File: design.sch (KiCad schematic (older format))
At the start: 21 parts, among them J1 USB_C_Receptacle, J2 Conn_01x05, Q1 2N7002K, Q2 2N7002K, Q3 2N7002K, U1 ATtiny814-SS

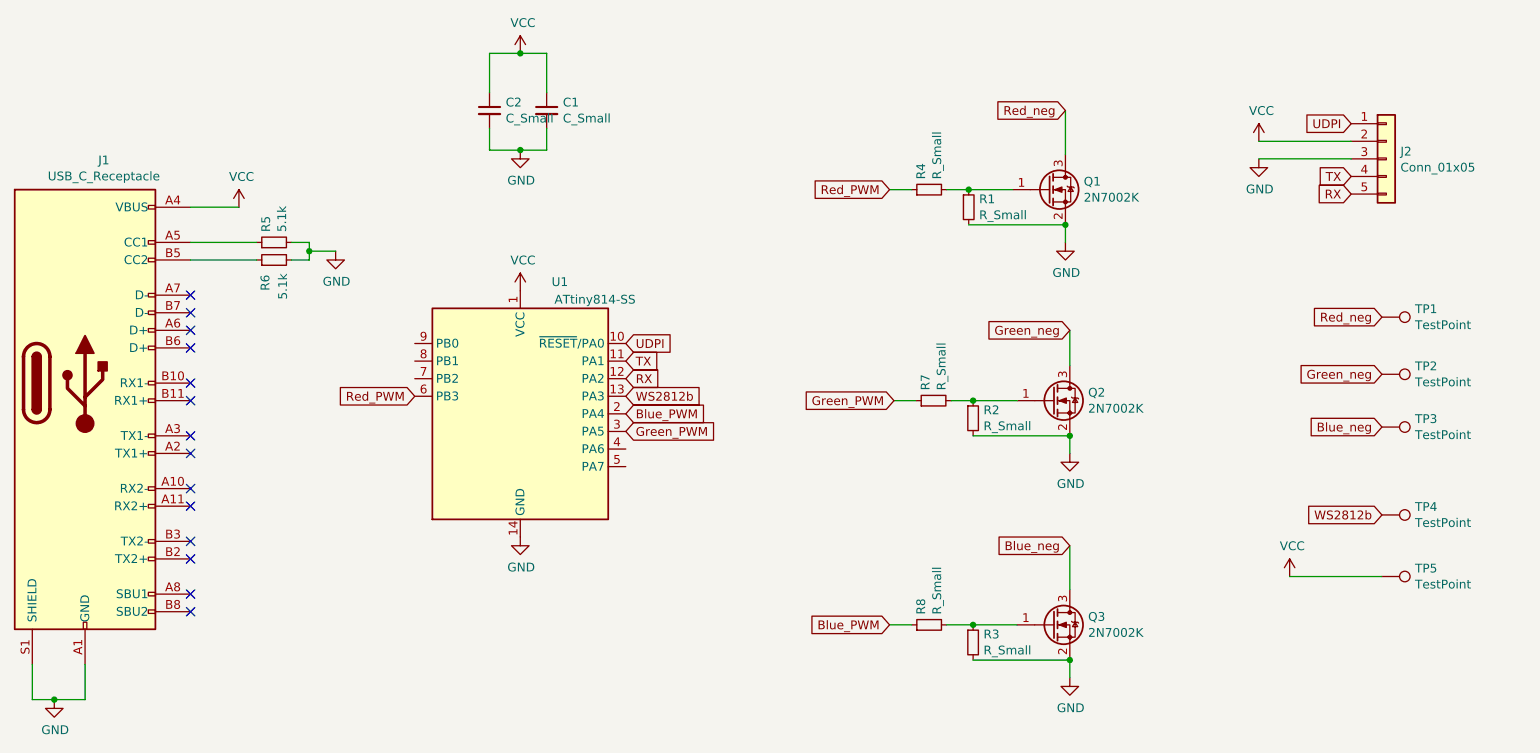
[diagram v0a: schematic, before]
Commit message: SCH: added values
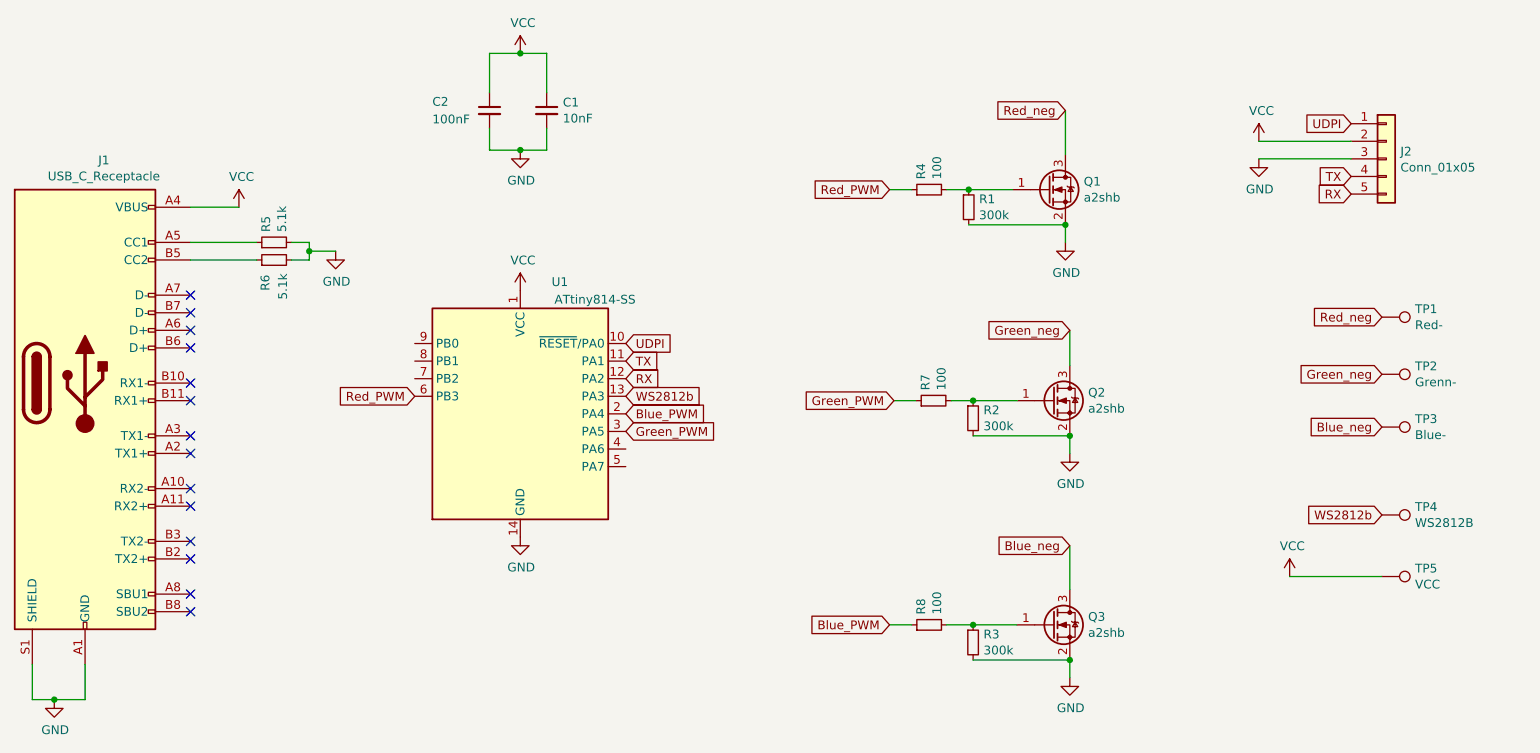
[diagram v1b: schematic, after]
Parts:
- C1: value C_Small -> 10nF
- C2: value C_Small -> 100nF
- Q1, Q2, Q3: value 2N7002K -> a2shb
- R1, R2, R3: value R_Small -> 300k
- R4, R7, R8: value R_Small -> 100
- TP1: value TestPoint -> Red-
- TP2: value TestPoint -> Grenn-
- TP3: value TestPoint -> Blue-
- TP4: value TestPoint -> WS2812B
- TP5: value TestPoint -> VCC
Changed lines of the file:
@@
 P 4725 2025
 F 0 "C1" H 4817 2071 50  0000 L CNN
-F 1 "C_Small" H 4817 1980 50  0000 L CNN
+F 1 "10nF" H 4817 1980 50  0000 L CNN
 F 2 "Capacitor_SMD:C_0805_2012Metric" H 4725 2025 50  0001 C CNN
 F 3 "~" H 4725 2025 50  0001 C CNN
@@
 U 1 1 616F58A4
 P 4400 2025
-F 0 "C2" H 4492 2071 50  0000 L CNN
-F 1 "C_Small" H 4492 1980 50  0000 L CNN
+F 0 "C2" H 4075 2075 50  0000 L CNN
+F 1 "100nF" H 4075 1975 50  0000 L CNN
 F 2 "Capacitor_SMD:C_0805_2012Metric" H 4400 2025 50  0001 C CNN
 F 3 "~" H 4400 2025 50  0001 C CNN
@@
 P 7575 2475
 F 0 "Q1" H 7779 2521 50  0000 L CNN
-F 1 "2N7002K" H 7779 2430 50  0000 L CNN
+F 1 "a2shb" H 7779 2430 50  0000 L CNN
 F 2 "Package_TO_SOT_SMD:SOT-23" H 7775 2400 50  0001 L CIN
 F 3 "https://www.diodes.com/assets/Datasheets/ds30896.pdf" H 7575 2475 50  0001 L CNN
@@
 P 7600 3675
 F 0 "Q2" H 7804 3721 50  0000 L CNN
-F 1 "2N7002K" H 7804 3630 50  0000 L CNN
+F 1 "a2shb" H 7804 3630 50  0000 L CNN
 F 2 "Package_TO_SOT_SMD:SOT-23" H 7800 3600 50  0001 L CIN
 F 3 "https://www.diodes.com/assets/Datasheets/ds30896.pdf" H 7600 3675 50  0001 L CNN
@@
 P 7600 4950
 F 0 "Q3" H 7804 4996 50  0000 L CNN
-F 1 "2N7002K" H 7804 4905 50  0000 L CNN
+F 1 "a2shb" H 7804 4905 50  0000 L CNN
 F 2 "Package_TO_SOT_SMD:SOT-23" H 7800 4875 50  0001 L CIN
 F 3 "https://www.diodes.com/assets/Datasheets/ds30896.pdf" H 7600 4950 50  0001 L CNN
@@
 P 7125 2575
 F 0 "R1" H 7184 2621 50  0000 L CNN
-F 1 "R_Small" H 7184 2530 50  0000 L CNN
+F 1 "300k" H 7184 2530 50  0000 L CNN
 F 2 "Resistor_SMD:R_0805_2012Metric" H 7125 2575 50  0001 C CNN
 F 3 "~" H 7125 2575 50  0001 C CNN
@@
 P 7150 3775
 F 0 "R2" H 7209 3821 50  0000 L CNN
-F 1 "R_Small" H 7209 3730 50  0000 L CNN
+F 1 "300k" H 7209 3730 50  0000 L CNN
 F 2 "Resistor_SMD:R_0805_2012Metric" H 7150 3775 50  0001 C CNN
 F 3 "~" H 7150 3775 50  0001 C CNN
@@
 P 7150 5050
 F 0 "R3" H 7209 5096 50  0000 L CNN
-F 1 "R_Small" H 7209 5005 50  0000 L CNN
+F 1 "300k" H 7209 5005 50  0000 L CNN
 F 2 "Resistor_SMD:R_0805_2012Metric" H 7150 5050 50  0001 C CNN
 F 3 "~" H 7150 5050 50  0001 C CNN
@@
 P 9475 3200
 F 0 "TP1" V 9429 3388 50  0000 L CNN
-F 1 "TestPoint" V 9520 3388 50  0000 L CNN
+F 1 "Red-" V 9520 3388 50  0000 L CNN
 F 2 "Connector_Wire:SolderWirePad_1x01_SMD_1x2mm" H 9675 3200 50  0001 C CNN
 F 3 "~" H 9675 3200 50  0001 C CNN
@@
 P 9475 3525
 F 0 "TP2" V 9429 3713 50  0000 L CNN
-F 1 "TestPoint" V 9520 3713 50  0000 L CNN
+F 1 "Grenn-" V 9520 3713 50  0000 L CNN
 F 2 "Connector_Wire:SolderWirePad_1x01_SMD_1x2mm" H 9675 3525 50  0001 C CNN
 F 3 "~" H 9675 3525 50  0001 C CNN
@@
 P 9475 3825
 F 0 "TP3" V 9429 4013 50  0000 L CNN
-F 1 "TestPoint" V 9520 4013 50  0000 L CNN
+F 1 "Blue-" V 9520 4013 50  0000 L CNN
 F 2 "Connector_Wire:SolderWirePad_1x01_SMD_1x2mm" H 9675 3825 50  0001 C CNN
 F 3 "~" H 9675 3825 50  0001 C CNN
@@
 P 9475 4325
 F 0 "TP4" V 9429 4513 50  0000 L CNN
-F 1 "TestPoint" V 9520 4513 50  0000 L CNN
+F 1 "WS2812B" V 9520 4513 50  0000 L CNN
 F 2 "Connector_Wire:SolderWirePad_1x01_SMD_1x2mm" H 9675 4325 50  0001 C CNN
 F 3 "~" H 9675 4325 50  0001 C CNN
@@
 P 6900 2475
 F 0 "R4" H 6959 2521 50  0000 L CNN
-F 1 "R_Small" H 6959 2430 50  0000 L CNN
+F 1 "100" H 6959 2430 50  0000 L CNN
 F 2 "Resistor_SMD:R_0805_2012Metric" H 6900 2475 50  0001 C CNN
 F 3 "~" H 6900 2475 50  0001 C CNN
@@
 P 6925 3675
 F 0 "R7" H 6984 3721 50  0000 L CNN
-F 1 "R_Small" H 6984 3630 50  0000 L CNN
+F 1 "100" H 6984 3630 50  0000 L CNN
 F 2 "Resistor_SMD:R_0805_2012Metric" H 6925 3675 50  0001 C CNN
 F 3 "~" H 6925 3675 50  0001 C CNN
@@
 P 6900 4950
 F 0 "R8" H 6959 4996 50  0000 L CNN
-F 1 "R_Small" H 6959 4905 50  0000 L CNN
+F 1 "100" H 6959 4905 50  0000 L CNN
 F 2 "Resistor_SMD:R_0805_2012Metric" H 6900 4950 50  0001 C CNN
 F 3 "~" H 6900 4950 50  0001 C CNN
@@
 P 9475 4675
 F 0 "TP5" V 9429 4863 50  0000 L CNN
-F 1 "TestPoint" V 9520 4863 50  0000 L CNN
+F 1 "VCC" V 9520 4863 50  0000 L CNN
 F 2 "Connector_Wire:SolderWirePad_1x01_SMD_1x2mm" H 9675 4675 50  0001 C CNN
 F 3 "~" H 9675 4675 50  0001 C CNN
@@
 $EndComp
 $Comp
-L power:VCC #PWR?
+L power:VCC #PWR0113
 U 1 1 61AAD6C9
 P 8950 4675
-F 0 "#PWR?" H 8950 4525 50  0001 C CNN
+F 0 "#PWR0113" H 8950 4525 50  0001 C CNN
 F 1 "VCC" H 8965 4848 50  0000 C CNN
 F 2 "" H 8950 4675 50  0001 C CNN

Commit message: SCH: added values
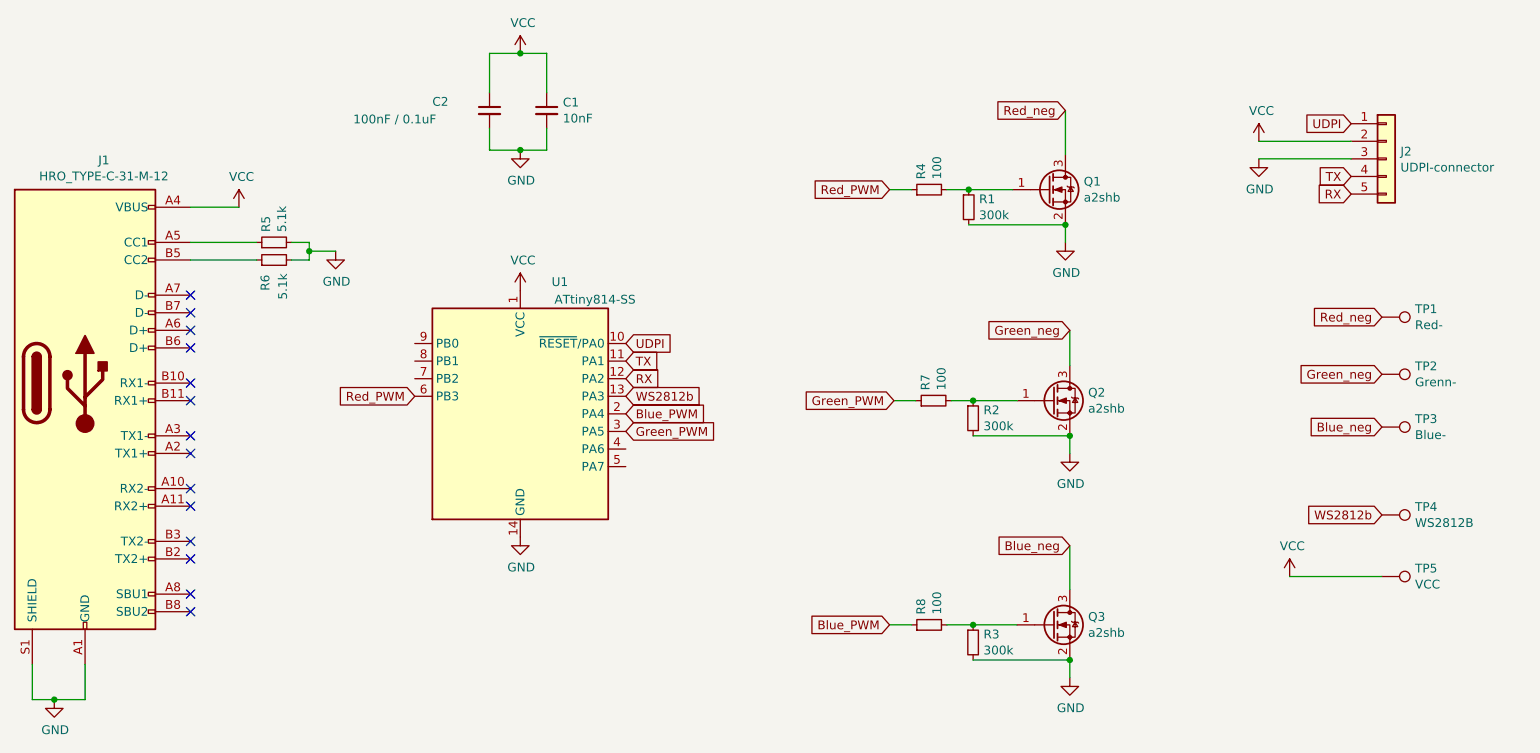
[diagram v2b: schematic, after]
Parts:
- C2: value 100nF -> 100nF / 0.1uF
- J1: value USB_C_Receptacle -> HRO_TYPE-C-31-M-12
- J2: value Conn_01x05 -> UDPI-connector
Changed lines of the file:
@@
 P 2100 3575
 F 0 "J1" H 2207 4842 50  0000 C CNN
-F 1 "USB_C_Receptacle" H 2207 4751 50  0000 C CNN
+F 1 "HRO_TYPE-C-31-M-12" H 2207 4751 50  0000 C CNN
 F 2 "Connector_USB:USB_C_Receptacle_HRO_TYPE-C-31-M-12_simple" H 2250 3575 50  0001 C CNN
 F 3 "https://www.usb.org/sites/default/files/documents/usb_type-c.zip" H 2250 3575 50  0001 C CNN
@@
 P 4400 2025
 F 0 "C2" H 4075 2075 50  0000 L CNN
-F 1 "100nF" H 4075 1975 50  0000 L CNN
+F 1 "100nF / 0.1uF" H 3625 1975 50  0000 L CNN
 F 2 "Capacitor_SMD:C_0805_2012Metric" H 4400 2025 50  0001 C CNN
 F 3 "~" H 4400 2025 50  0001 C CNN
@@
 P 9500 2300
 F 0 "J2" H 9580 2342 50  0000 L CNN
-F 1 "Conn_01x05" H 9580 2251 50  0000 L CNN
+F 1 "UDPI-connector" H 9580 2251 50  0000 L CNN
 F 2 "E32-xxxT20D:UDPI_interface_small" H 9500 2300 50  0001 C CNN
 F 3 "~" H 9500 2300 50  0001 C CNN
